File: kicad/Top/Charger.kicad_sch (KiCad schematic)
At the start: 37 parts

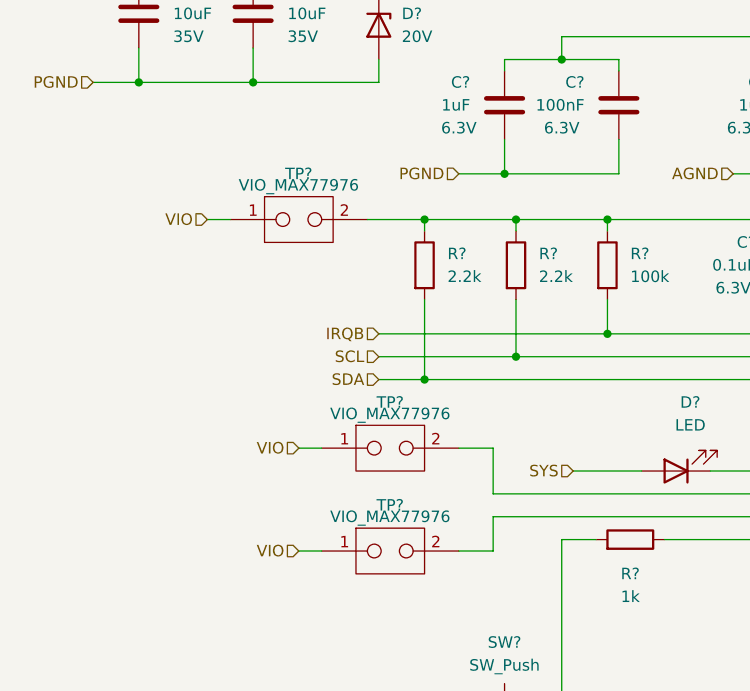
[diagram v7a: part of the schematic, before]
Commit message: Updated shunt naming and references to better convey default connections
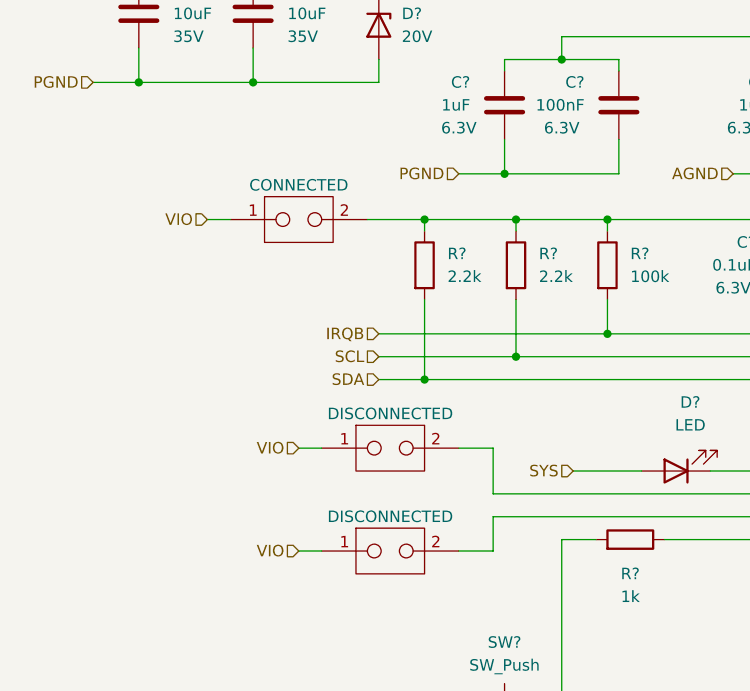
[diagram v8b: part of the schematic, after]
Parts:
- removed TP? (x2): VIO_MAX77976, custom_connectors:2.54mm_2pointCurrentTestPoint, symbol custom_connectors:TestPoint_CurrentShunt
- added CHG_DISQBAT, CHG_SUSPND: DISCONNECTED, custom_connectors:2.54mm_2pointCurrentTestPoint, symbol custom_connectors:TestPoint_CurrentShunt
- CHG_VIO: renamed from TP?; value VIO_MAX77976 -> CONNECTED; Populated Yes -> (none)
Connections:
- net VIO: now also CHG_DISQBAT.1, CHG_SUSPND.1
- net at U?.1 (DISQBAT): now also CHG_DISQBAT.2
- net at U?.31 (SUSPND): now also CHG_SUSPND.2
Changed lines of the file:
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@@
     (effects (font (size 1.27 1.27)) (justify right))
   )
+  (symbol (lib_id "custom_connectors:TestPoint_CurrentShunt") (at 45.72 146.05 0) (unit 1)
+    (in_bom yes) (on_board yes) (fields_autoplaced)
+    (property "Reference" "CHG_DISQBAT" (id 0) (at 45.72 140.97 0)
+      (effects (font (size 1.27 1.27)) hide)
+    )
+    (property "Value" "DISCONNECTED" (id 1) (at 45.72 142.24 0))
+    (property "Footprint" "custom_connectors:2.54mm_2pointCurrentTestPoint" (id 2) (at 45.72 146.05 0)
+      (effects (font (size 1.27 1.27)) hide)
+    )
+    (property "Datasheet" "https://www.digikey.jp/product-detail/en/kycon-inc/SX1100-B/2092-SX1100-B-ND/9990206" (id 3) (at 45.72 146.05 0)
+      (effects (font (size 1.27 1.27)) hide)
+    )
+    (pin "1")
+    (pin "2")
+  )
   (symbol (lib_id "Device:C") (at 191.77 128.27 0) (mirror y) (unit 1)
     (in_bom yes) (on_board yes) (fields_autoplaced)
@@
     )
     (property "Description" "6.3V" (id 4) (at 85.09 99.06 0))
-    (pin "1")
-    (pin "2")
-  )
-  (symbol (lib_id "custom_connectors:TestPoint_CurrentShunt") (at 45.72 146.05 0) (unit 1)
-    (in_bom yes) (on_board yes) (fields_autoplaced)
-    (property "Reference" "TP?" (id 0) (at 45.72 140.97 0))
-    (property "Value" "VIO_MAX77976" (id 1) (at 45.72 142.24 0))
-    (property "Footprint" "custom_connectors:2.54mm_2pointCurrentTestPoint" (id 2) (at 45.72 146.05 0)
-      (effects (font (size 1.27 1.27)) hide)
-    )
-    (property "Datasheet" "https://www.digikey.jp/product-detail/en/kycon-inc/SX1100-B/2092-SX1100-B-ND/9990206" (id 3) (at 45.72 146.05 0)
-      (effects (font (size 1.27 1.27)) hide)
-    )
-    (property "Default" "Disconnected" (id 13) (at 45.72 146.05 0)
-      (effects (font (size 1.27 1.27)) hide)
-    )
     (pin "1")
     (pin "2")
@@
     )
     (property "Description" "16V 1210 100uF" (id 4) (at 255.27 105.41 0))
-    (pin "1")
-    (pin "2")
-  )
-  (symbol (lib_id "custom_connectors:TestPoint_CurrentShunt") (at 45.72 134.62 0) (unit 1)
-    (in_bom yes) (on_board yes) (fields_autoplaced)
-    (property "Reference" "TP?" (id 0) (at 45.72 129.54 0))
-    (property "Value" "VIO_MAX77976" (id 1) (at 45.72 130.81 0))
-    (property "Footprint" "custom_connectors:2.54mm_2pointCurrentTestPoint" (id 2) (at 45.72 134.62 0)
-      (effects (font (size 1.27 1.27)) hide)
-    )
-    (property "Datasheet" "https://www.digikey.jp/product-detail/en/kycon-inc/SX1100-B/2092-SX1100-B-ND/9990206" (id 3) (at 45.72 134.62 0)
-      (effects (font (size 1.27 1.27)) hide)
-    )
-    (property "Populated" "No" (id 4) (at 45.72 134.62 0)
-      (effects (font (size 1.27 1.27)) hide)
-    )
     (pin "1")
     (pin "2")
@@
   (symbol (lib_id "custom_connectors:TestPoint_CurrentShunt") (at 35.56 109.22 0) (unit 1)
     (in_bom yes) (on_board yes) (fields_autoplaced)
-    (property "Reference" "TP?" (id 0) (at 35.56 104.14 0))
-    (property "Value" "VIO_MAX77976" (id 1) (at 35.56 105.41 0))
+    (property "Reference" "CHG_VIO" (id 0) (at 35.56 104.14 0)
+      (effects (font (size 1.27 1.27)) hide)
+    )
+    (property "Value" "CONNECTED" (id 1) (at 35.56 105.41 0))
     (property "Footprint" "custom_connectors:2.54mm_2pointCurrentTestPoint" (id 2) (at 35.56 109.22 0)
       (effects (font (size 1.27 1.27)) hide)
     )
     (property "Datasheet" "https://www.digikey.jp/product-detail/en/kycon-inc/SX1100-B/2092-SX1100-B-ND/9990206" (id 3) (at 35.56 109.22 0)
-      (effects (font (size 1.27 1.27)) hide)
-    )
-    (property "Populated" "Yes" (id 4) (at 35.56 109.22 0)
       (effects (font (size 1.27 1.27)) hide)
     )
@@
     (pin "1")
     (pin "2")
+  )
+  (symbol (lib_id "custom_connectors:TestPoint_CurrentShunt") (at 45.72 134.62 0) (unit 1)
+    (in_bom yes) (on_board yes) (fields_autoplaced)
+    (property "Reference" "CHG_SUSPND" (id 0) (at 45.72 129.54 0)
+      (effects (font (size 1.27 1.27)) hide)
+    )
+    (property "Value" "DISCONNECTED" (id 1) (at 45.72 130.81 0))
+    (property "Footprint" "custom_connectors:2.54mm_2pointCurrentTestPoint" (id 2) (at 45.72 134.62 0)
+      (effects (font (size 1.27 1.27)) hide)
+    )
+    (property "Datasheet" "https://www.digikey.jp/product-detail/en/kycon-inc/SX1100-B/2092-SX1100-B-ND/9990206" (id 3) (at 45.72 134.62 0)
+      (effects (font (size 1.27 1.27)) hide)
+    )
+    (pin "1")
+    (pin "2")
